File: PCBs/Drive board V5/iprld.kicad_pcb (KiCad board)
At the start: 2 copper layers, 100 x 60 mm, 14 parts, among them J1 Conn_01x02, J2 Conn_02x01, J3 Conn_02x02_Top_Bottom, U1 TJA1051T-3

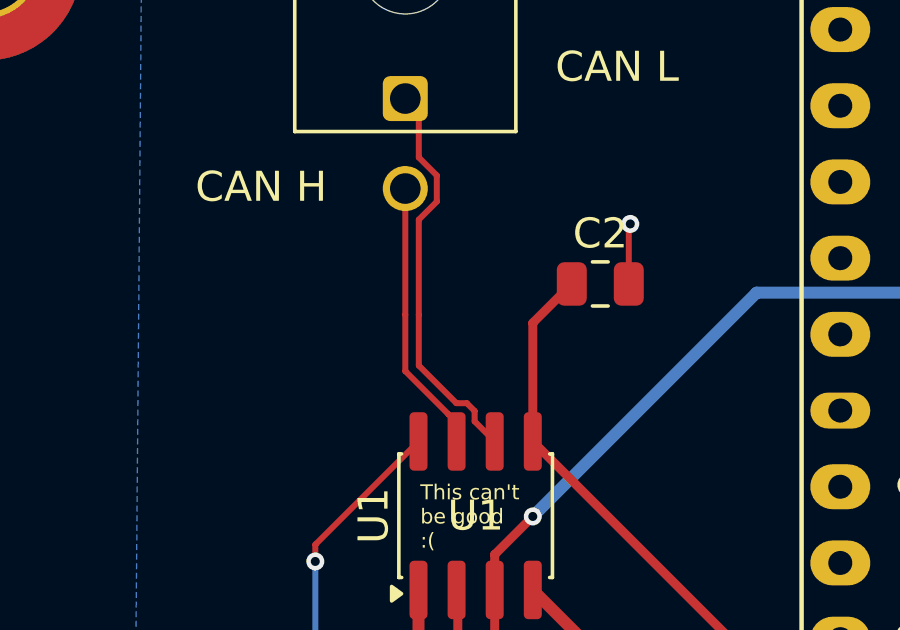
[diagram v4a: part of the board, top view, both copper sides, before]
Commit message: Added termination resistor to drive
Can be used in event that drive board is used as one end of can bus
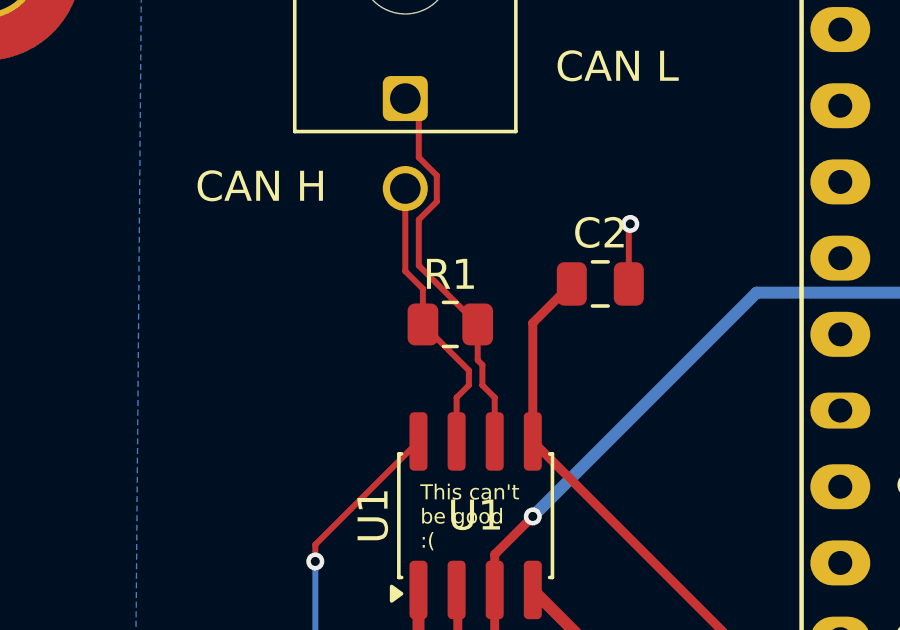
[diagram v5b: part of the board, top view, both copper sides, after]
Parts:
- added R1: 120, Resistor_SMD:R_0805_2012Metric, F.Cu at (40.5, 37.0)
